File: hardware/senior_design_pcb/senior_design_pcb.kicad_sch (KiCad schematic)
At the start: 62 parts, among them J1 SBH11-PBPC-D05-ST-BK, J10 Screw_Terminal_01x06, J11 Conn_02x08_Odd_Even, J12 Conn_01x05_Socket, J2 USB_C_Receptacle_USB2.0_16P, J3 Conn_01x02_Socket, J4 Conn_01x03_Socket, J5 Conn_01x05_Socket, J6 Conn_01x05_Socket, J7 Conn_01x02_Socket, J8 Conn_01x03_Socket, J9 Screw_Terminal_01x06, SW2 SW_Push, SW3 SW_Push, SW4 SW_Push, U1 FT232RL, U2 STM32F091RCTx, U3 LD1117S33TR_SOT223, U4 KMR241GLFS

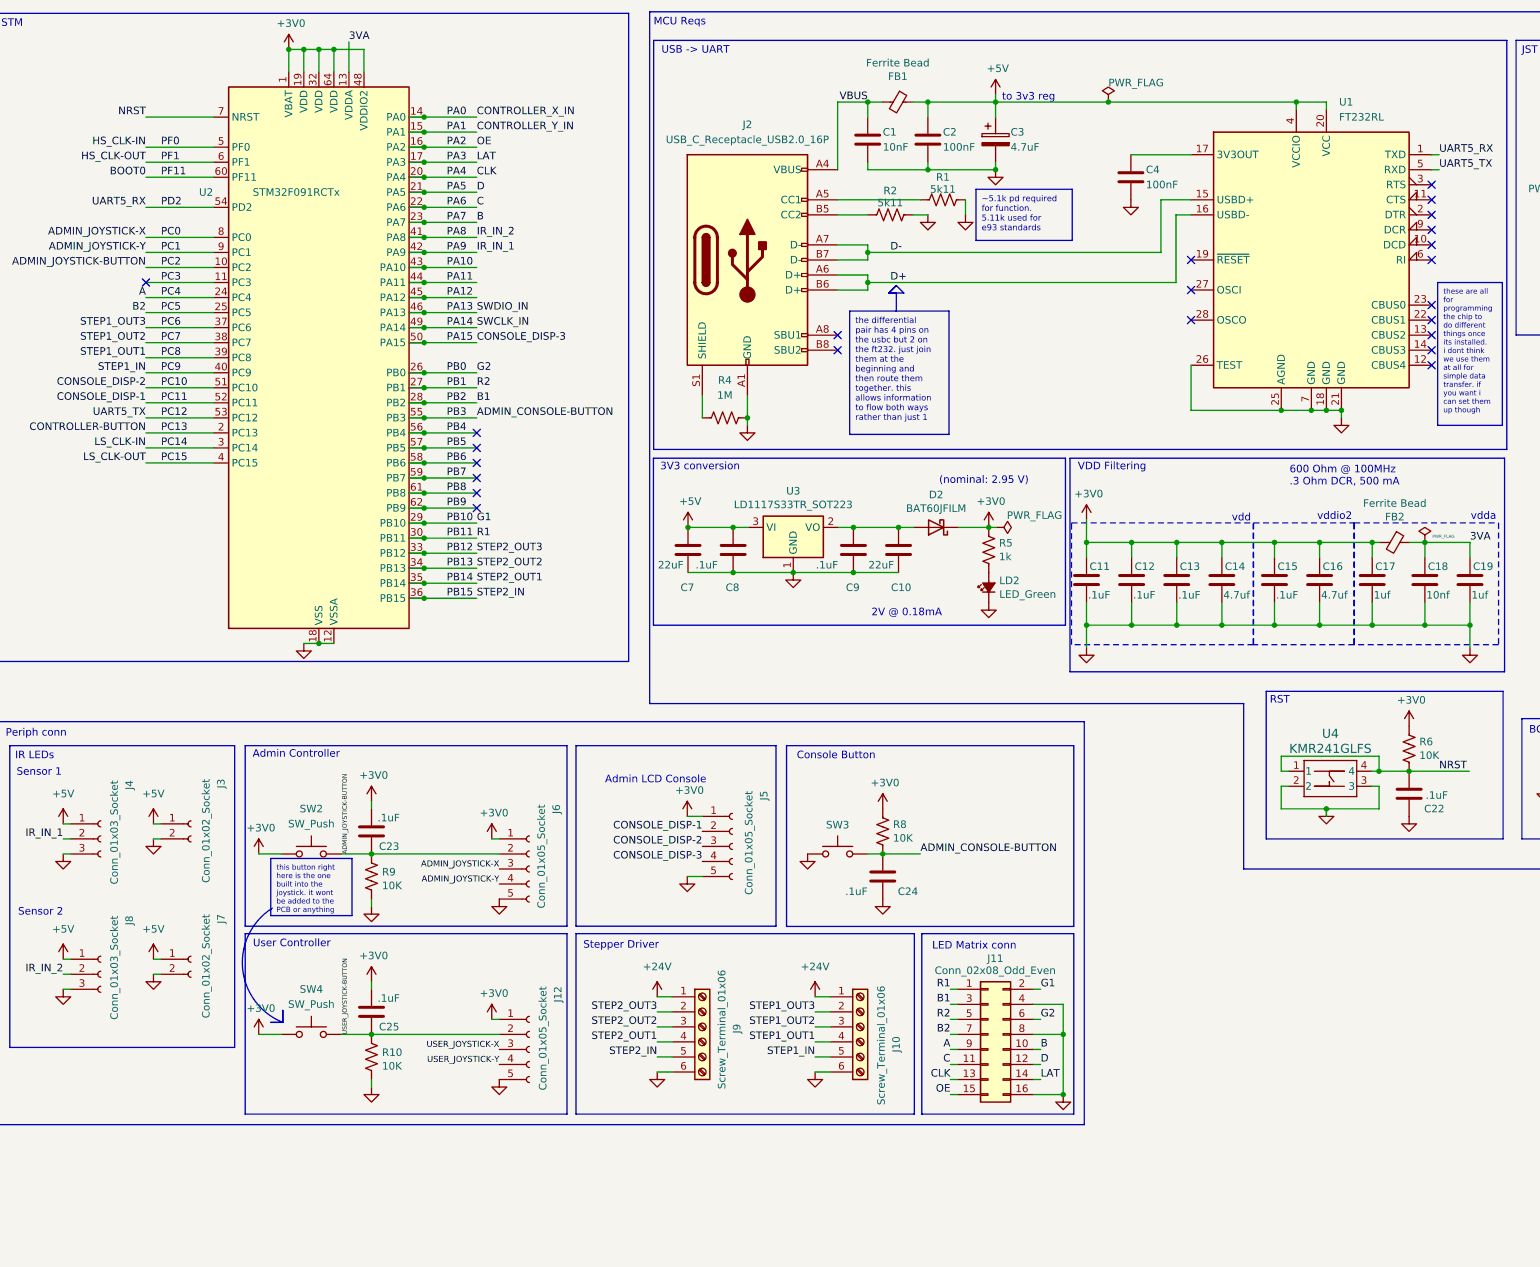
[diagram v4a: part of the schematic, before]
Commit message: organized components
added labels
grouped
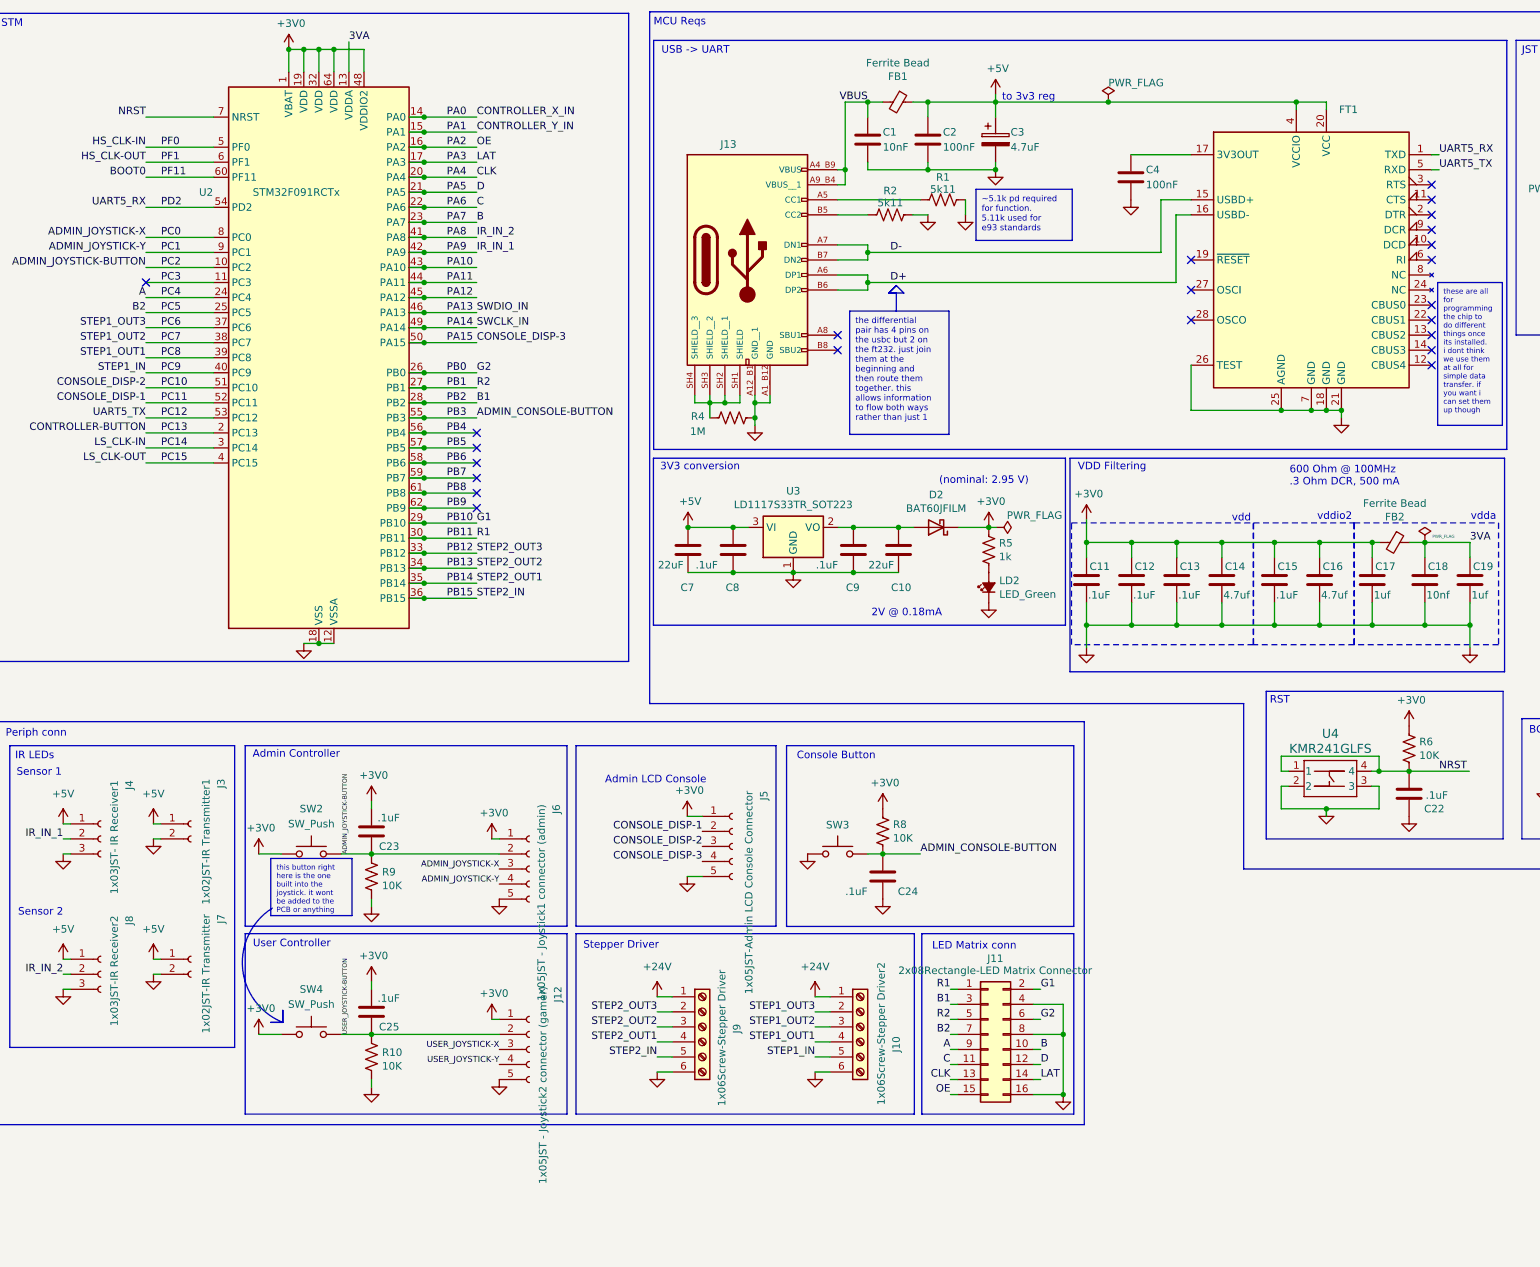
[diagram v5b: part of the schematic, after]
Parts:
- removed J2: USB_C_Receptacle_USB2.0_16P, Sr_ Design:USB-C-PORT-2, symbol Connector:USB_C_Receptacle_USB2.0_16P
- removed U1: FT232RL, Package_SO:SSOP-28_5.3x10.2mm_P0.65mm, symbol Interface_USB:FT232RL
- added FT1: ~, Package_SO:SSOP-28_5.3x10.2mm_P0.65mm, symbol FT232-CUSTOM:ft232-custom-lolf
- added J13: UJ20-C-H-C-4-SMT-TR, Sr_ Design:USB-C-PORT-2, symbol USB-C-PORT-2:UJ20-C-H-C-4-SMT-TR
- J10: value Screw_Terminal_01x06 -> 1x06Screw-Stepper Driver2
- J11: value Conn_02x08_Odd_Even -> 2x08Rectangle-LED Matrix Connector
- J12: value Conn_01x05_Socket -> 1x05JST - Joystick2 connector (gamer)
- J3: value Conn_01x02_Socket -> 1x02JST-IR Transmitter1
- J4: value Conn_01x03_Socket -> 1x03JST- IR Receiver1
- J5: value Conn_01x05_Socket -> 1x05JST-Admin LCD Console Connector
- J6: value Conn_01x05_Socket -> 1x05JST - Joystick1 connector (admin)
- J7: value Conn_01x02_Socket -> 1x02JST-IR Transmitter
- J8: value Conn_01x03_Socket -> 1x03JST-IR Receiver2
- J9: value Screw_Terminal_01x06 -> 1x06Screw-Stepper Driver
- SW3: value SW_Push -> 1x02JST-Admin Console button connector
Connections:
- net +5V: now also FT1.20 (VCC), FT1.4 (VCCIO)
- net D+: now also FT1.16 (USBD-), J13.A6 (DP1), J13.B6 (DP2)
- net D-: now also FT1.15 (USBD+), J13.A7 (DN1), J13.B7 (DN2)
- net GND: now also FT1.18 (GND), FT1.21 (GND), FT1.25 (AGND), FT1.26 (TEST), FT1.7 (GND), J13.A12_B1 (GND__1), J13.A1_B12 (GND)
- net PC12: now also FT1.5 (RXD)
- net PD2: now also FT1.1 (TXD)
- net VBUS: now also J13.A4_B9 (VBUS), J13.A9_B4 (VBUS__1)
- net at C4.1: now also FT1.17 (3V3OUT)
- net at R1.1: now also J13.A5 (CC1)
- net at R2.1: now also J13.B5 (CC2)
- net at R4.1: now also J13.SH1 (SHIELD), J13.SH2 (SHIELD__1), J13.SH3 (SHIELD__2), J13.SH4 (SHIELD__3)
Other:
- moved on the sheet: R4

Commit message: edited layout
made it more finalized, some changes needed still.
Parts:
- C1: value 10nF -> .01uF
- C18: value 10nf -> .01uF
- C2, C4: value 100nF -> .1uF
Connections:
- net USER_JOYSTICK-BUTTON is gone; now on net PC13: C25.2, J12.2 (Pin_2), R10.1, SW4.2
- net USER_JOYSTICK-X is gone; now on net PA0: J12.3 (Pin_3)
- net USER_JOYSTICK-Y is gone; now on net PA1: J12.4 (Pin_4)
- net 3v3-vo: now reaches C10.1, C9.1, D2.2 (A), U3.2 (VO)
- net CONTROLLER-BUTTON renamed PC13
- net CONTROLLER_X_IN renamed PA0
- net CONTROLLER_Y_IN renamed PA1
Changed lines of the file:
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@@
 		)
 	)
+	(label "USER_JOYSTICK-X"
+		(at 95.25 31.75 0)
+		(effects
+			(font
+				(size 1.016 1.016)
+			)
+			(justify left bottom)
+		)
+	)
 	(label "B1"
 		(at 175.26 181.61 180)
@@
 		)
 	)
-	(label "CONTROLLER_X_IN"
-		(at 95.25 31.75 0)
-		(effects
-			(font
-				(size 1.27 1.27)
-			)
-			(justify left bottom)
-		)
-	)
-	(label "CONTROLLER-BUTTON"
-		(at 39.37 85.09 180)
-		(effects
-			(font
-				(size 1.27 1.27)
-			)
-			(justify right bottom)
-		)
-	)
 	(label "CLK"
 		(at 95.25 41.91 0)
@@
 		)
 	)
+	(label "3v3-vo"
+		(at 160.02 101.0543 0)
+		(effects
+			(font
+				(size 1.27 1.27)
+			)
+			(justify left bottom)
+		)
+	)
 	(label "PC15"
 		(at 316.23 111.76 0)
@@
 		)
 	)
-	(label "CONTROLLER_Y_IN"
-		(at 95.25 34.29 0)
-		(effects
-			(font
-				(size 1.27 1.27)
-			)
-			(justify left bottom)
-		)
-	)
 	(label "STEP2_OUT2"
 		(at 95.25 107.95 0)
@@
 		)
 	)
+	(label "USER_JOYSTICK-BUTTON"
+		(at 39.37 85.09 180)
+		(effects
+			(font
+				(size 0.762 0.762)
+			)
+			(justify right bottom)
+		)
+	)
 	(label "PA12"
 		(at 90.17 62.23 0)
@@
 		)
 	)
+	(label "USER_JOYSTICK-Y"
+		(at 95.25 34.29 0)
+		(effects
+			(font
+				(size 1.016 1.016)
+			)
+			(justify left bottom)
+		)
+	)
 	(label "PB1"
 		(at 90.17 77.47 0)
@@
 			)
 		)
-		(property "Value" "10nf"
+		(property "Value" ".01uF"
 			(at 255.647 112.4843 0)
 			(effects
@@
 			)
 		)
-		(property "Value" "100nF"
+		(property "Value" ".1uF"
 			(at 208.28 43.18 0)
 			(effects
@@
 			)
 		)
-		(property "Value" "100nF"
+		(property "Value" ".1uF"
 			(at 173.99 36.83 0)
 			(effects
@@
 			)
 		)
-		(property "Value" "10nF"
+		(property "Value" ".01uF"
 			(at 163.83 36.83 0)
 			(effects

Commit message: cleaned it up
added comments and added squares.
reorganized into more precise rectangles
marked extra requirements
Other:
- note added: "3V3 reg"
- note added: "3v3 Status LED"
- note added: "Communications"
- note added: "FT232 USB-UART bridge"
- note added: "IR Sensors"
- note added: "PC14 = LSE CLK - in PC15 = LSE CLK - out"
- note added: "PF0 = HSE CLK - in PF1 = HSE CLK - out"
- note added: "Peripheral signal connectors (all externally powered)"
- note added: "Power"
- note added: "Reset button"
- note added: "Stretch Requirements"
- note added: "USB-C port"
- note added: "external clocks"
- note added: "one for each pin connected to VDD, 4.7uF bulk caps near source"
- note added: "should we have a clock select jumper like the 362 board?"
- note removed: "(nominal: 2.95 V)"
- note removed: "2V @ 0.18mA"
- note removed: "3V3 conversion"
- note removed: "IR LEDs"
- note removed: "MCU Reqs"
- note removed: "Periph conn"
- moved on the sheet: C1, C10, C11, C12, C13, C14, C15, C16, C17, C18, C19, C2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

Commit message: added comments
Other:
- moved on the sheet: C10, C11, C12, C13, C14, C15, C16, C17, C18, C19, C22, C7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
